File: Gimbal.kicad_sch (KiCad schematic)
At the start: 41 parts, among them J1 Conn_01x03, J2 USB_C_Receptacle_USB2.0, J3 0022232041, J4 0022232041, J5 0022232041, J6 Conn_01x02, Q1 Q_NPN_BCE, Q2 Q_NPN_BCE, SW1 SW_Push, U1 ESP32-WROOM-32U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

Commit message: draft submission
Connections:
- net RX renamed ESPRX
- net ESPRX: now also U3.26 (TXD); no longer U3.25 (RXD)
- net TX renamed ESPTX
- net ESPTX: now also U3.25 (RXD); no longer U3.26 (TXD)
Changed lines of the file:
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@@
     (effects (font (size 1.27 1.27)) (justify left bottom))
   )
-  (label "RX" (at 379.73 134.62 90)
+  (label "ESPRX" (at 379.73 134.62 90)
     (effects (font (size 1.27 1.27)) (justify left bottom))
   )
@@
     (effects (font (size 1.27 1.27)) (justify right bottom))
   )
-  (label "RX" (at 128.27 312.42 0)
+  (label "ESPTX" (at 128.27 312.42 0)
     (effects (font (size 1.27 1.27)) (justify left bottom))
   )
@@
     (effects (font (size 1.27 1.27)) (justify left bottom))
   )
-  (label "TX" (at 71.12 214.63 0)
+  (label "ESPTX" (at 71.12 214.63 0)
     (effects (font (size 1.27 1.27)) (justify left bottom))
   )
@@
     (effects (font (size 1.27 1.27)) (justify left bottom))
   )
-  (label "TX" (at 128.27 309.88 0)
+  (label "ESPRX" (at 128.27 309.88 0)
     (effects (font (size 1.27 1.27)) (justify left bottom))
   )
@@
     (effects (font (size 1.27 1.27)) (justify left bottom))
   )
-  (label "TX" (at 382.27 134.62 90)
+  (label "ESPTX" (at 382.27 134.62 90)
     (effects (font (size 1.27 1.27)) (justify left bottom))
   )
@@
     (effects (font (size 1.27 1.27)) (justify left bottom))
   )
-  (label "RX" (at 71.12 219.71 0)
+  (label "ESPRX" (at 71.12 219.71 0)
     (effects (font (size 1.27 1.27)) (justify left bottom))
   )

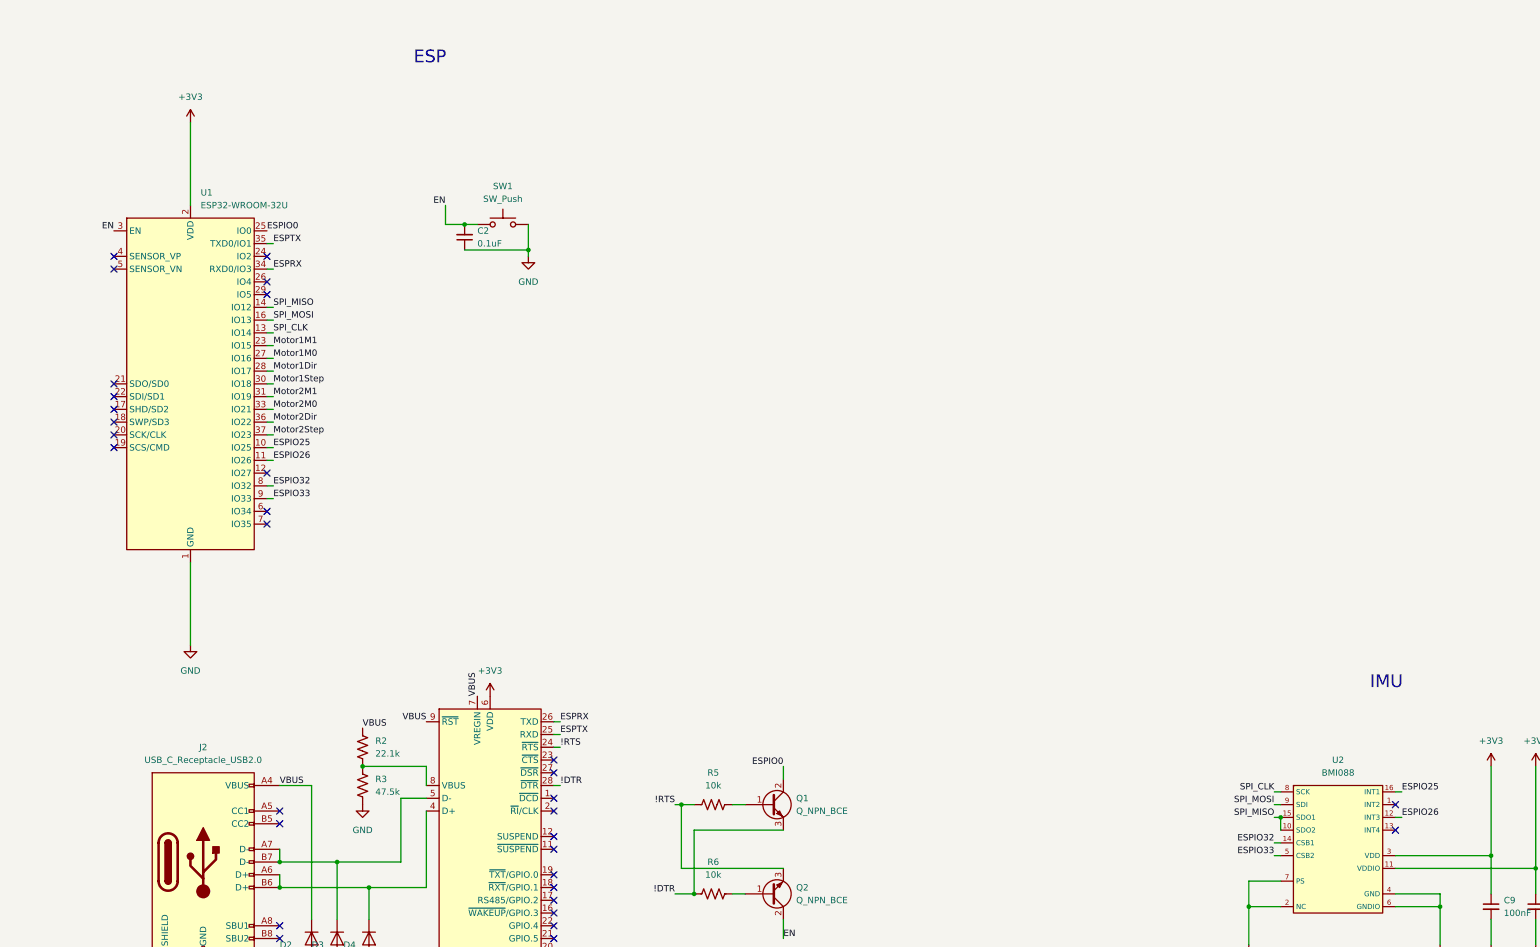
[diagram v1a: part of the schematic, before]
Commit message: changed esp to solo s2
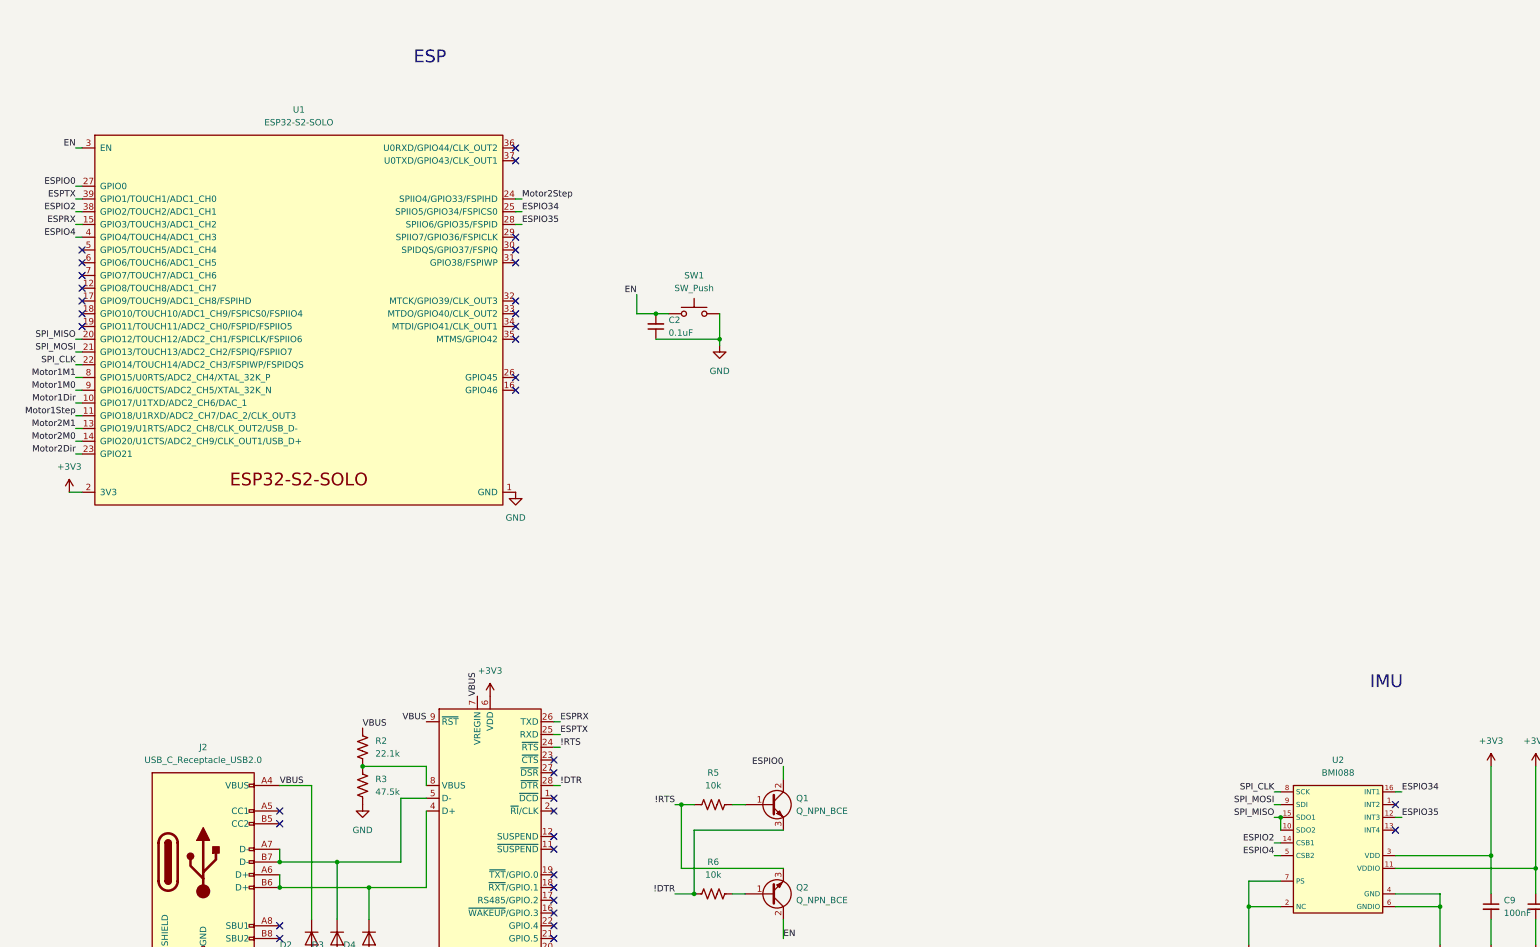
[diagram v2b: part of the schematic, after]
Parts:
- removed U1: ESP32-WROOM-32U, RF_Module:ESP32-WROOM-32U, symbol RF_Module:ESP32-WROOM-32U
- added U1: ESP32-S2-SOLO, Espressif:ESP32-S2-SOLO, symbol Espressif:ESP32-S2-SOLO
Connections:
- net +3V3: now also U1.2 (3V3)
- net EN: now also U1.3 (EN)
- net ESPIO0: now also U1.27 (GPIO0)
- net ESPRX: now also U1.15 (GPIO3/TOUCH3/ADC1_CH2)
- net ESPTX: now also U1.39 (GPIO1/TOUCH1/ADC1_CH0)
- net GND: now also U1.1 (GND), U1.40 (GND), U1.41 (GND)
- net Motor1Dir: now also U1.10 (GPIO17/U1TXD/ADC2_CH6/DAC_1)
- net Motor1M0: now also U1.9 (GPIO16/U0CTS/ADC2_CH5/XTAL_32K_N)
- net Motor1M1: now also U1.8 (GPIO15/U0RTS/ADC2_CH4/XTAL_32K_P)
- net Motor1Step: now also U1.11 (GPIO18/U1RXD/ADC2_CH7/DAC_2/CLK_OUT3)
- net Motor2Dir: now also U1.23 (GPIO21)
- net Motor2M0: now also U1.14 (GPIO20/U1CTS/ADC2_CH9/CLK_OUT1/USB_D+)
- net Motor2M1: now also U1.13 (GPIO19/U1RTS/ADC2_CH8/CLK_OUT2/USB_D-)
- net Motor2Step: now also U1.24 (SPIIO4/GPIO33/FSPIHD)
- net SPI_CLK: now also U1.22 (GPIO14/TOUCH14/ADC2_CH3/FSPIWP/FSPIDQS)
- net SPI_MISO: now also U1.20 (GPIO12/TOUCH12/ADC2_CH1/FSPICLK/FSPIIO6)
- net SPI_MOSI: now also U1.21 (GPIO13/TOUCH13/ADC2_CH2/FSPIQ/FSPIIO7)
- net ESPIO25 renamed ESPIO34
- net ESPIO34: now also U1.25 (SPIIO5/GPIO34/FSPICS0)
- net ESPIO26 renamed ESPIO35
- net ESPIO35: now also U1.28 (SPIIO6/GPIO35/FSPID)
- net ESPIO32 renamed ESPIO2
- net ESPIO2: now also U1.38 (GPIO2/TOUCH2/ADC1_CH1)
- net ESPIO33 renamed ESPIO4
- net ESPIO4: now also U1.4 (GPIO4/TOUCH4/ADC1_CH3)
- no-connect marks 54 -> 58
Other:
- moved on the sheet: C2, SW1

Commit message: assigned all footprints
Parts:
- C1, C10, C11, C2, C3, C4, C5, C6, C7, C8, C9: footprint (none) -> Capacitor_SMD:C_0805_2012Metric
- D1: footprint (none) -> Diode_SMD:D_SOD-323
- D2, D3, D4: footprint (none) -> Package_TO_SOT_SMD:SOT-143
- D5: footprint (none) -> LED_SMD:LED_0805_2012Metric
- J1: footprint (none) -> Connector_Molex:Molex_Micro-Fit_3.0_43650-0300_1x03_P3.00mm_Horizontal
- J2: footprint (none) -> Connector_USB:USB_C_Receptacle_Amphenol_12401548E4-2A
- J3, J4: footprint digikey-footprints:PinHeader_1x4_P2.54mm_Drill1.02mm -> Connector_Molex:Molex_KK-396_A-41791-0004_1x04_P3.96mm_Vertical
- J5: footprint digikey-footprints:PinHeader_1x4_P2.54mm_Drill1.02mm -> Connector_PinHeader_1.00mm:PinHeader_1x04_P1.00mm_Horizontal
- J6: footprint (none) -> Connector_PinHeader_1.00mm:PinHeader_1x02_P1.00mm_Horizontal
- Q1, Q2, U4: footprint (none) -> Package_TO_SOT_SMD:TSOT-23
- R1, R10, R2, R3, R4, R5, R6, R7, R8, R9: footprint (none) -> Resistor_SMD:R_0805_2012Metric
- SW1: footprint (none) -> Button_Switch_SMD:SW_Push_1P1T_NO_CK_KMR2
- U1: footprint Espressif:ESP32-S2-SOLO -> ESP32:ESP32-S2-SOLO
- U5, U6: footprint (none) -> DRV8846RGET:QFN50P400X400X100-25N

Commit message: routing actually good
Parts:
- J2: footprint Connector_USB:USB_C_Receptacle_Amphenol_12401548E4-2A -> Connector_USB:USB_C_Receptacle_Amphenol_12401610E4-2A
- J5: footprint Connector_PinHeader_1.00mm:PinHeader_1x04_P1.00mm_Horizontal -> Connector_PinHeader_2.00mm:PinHeader_1x04_P2.00mm_Horizontal
- J6: footprint Connector_PinHeader_1.00mm:PinHeader_1x02_P1.00mm_Horizontal -> Connector_PinHeader_2.00mm:PinHeader_1x02_P2.00mm_Horizontal
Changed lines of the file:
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@@
     (property "Reference" "J5" (id 0) (at 361.95 143.51 0))
     (property "Value" "0022232041" (id 1) (at 361.95 146.05 0))
-    (property "Footprint" "Connector_PinHeader_1.00mm:PinHeader_1x04_P1.00mm_Horizontal" (id 2) (at 363.22 133.35 0)
+    (property "Footprint" "Connector_PinHeader_2.00mm:PinHeader_1x04_P2.00mm_Horizontal" (id 2) (at 363.22 133.35 0)
       (effects (font (size 1.524 1.524)) (justify left) hide)
     )
@@
       (effects (font (size 1.27 1.27)) (justify left))
     )
-    (property "Footprint" "Connector_PinHeader_1.00mm:PinHeader_1x02_P1.00mm_Horizontal" (id 2) (at 382.27 139.7 0)
+    (property "Footprint" "Connector_PinHeader_2.00mm:PinHeader_1x02_P2.00mm_Horizontal" (id 2) (at 382.27 139.7 0)
       (effects (font (size 1.27 1.27)) hide)
     )
@@
     (property "Reference" "J2" (id 0) (at 57.15 314.96 0))
     (property "Value" "USB_C_Receptacle_USB2.0" (id 1) (at 57.15 317.5 0))
-    (property "Footprint" "Connector_USB:USB_C_Receptacle_Amphenol_12401548E4-2A" (id 2) (at 60.96 337.82 0)
+    (property "Footprint" "Connector_USB:USB_C_Receptacle_Amphenol_12401610E4-2A" (id 2) (at 60.96 337.82 0)
       (effects (font (size 1.27 1.27)) hide)
     )
@@
     )
     (path "/fea1b2d6-14bd-42c1-b173-7589da50729c"
-      (reference "J2") (unit 1) (value "USB_C_Receptacle_USB2.0") (footprint "Connector_USB:USB_C_Receptacle_Amphenol_12401548E4-2A")
+      (reference "J2") (unit 1) (value "USB_C_Receptacle_USB2.0") (footprint "Connector_USB:USB_C_Receptacle_Amphenol_12401610E4-2A")
     )
     (path "/74ab90dc-5bb1-43a8-b284-592b8a08facf"
@@
     )
     (path "/3aa960a7-fd3e-4e4f-9969-73f798fee9d8"
-      (reference "J5") (unit 1) (value "0022232041") (footprint "Connector_PinHeader_1.00mm:PinHeader_1x04_P1.00mm_Horizontal")
+      (reference "J5") (unit 1) (value "0022232041") (footprint "Connector_PinHeader_2.00mm:PinHeader_1x04_P2.00mm_Horizontal")
     )
     (path "/edaf7130-650f-465e-ad0d-68c5743db343"
-      (reference "J6") (unit 1) (value "Conn_01x02") (footprint "Connector_PinHeader_1.00mm:PinHeader_1x02_P1.00mm_Horizontal")
+      (reference "J6") (unit 1) (value "Conn_01x02") (footprint "Connector_PinHeader_2.00mm:PinHeader_1x02_P2.00mm_Horizontal")
     )
     (path "/0263937c-fc21-468b-8423-5c4cfc58d4c0"

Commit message: new schematic
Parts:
- removed D3, D4: DIODE, Package_TO_SOT_SMD:SOT-143, symbol Simulation_SPICE:DIODE
- removed J1: Conn_01x03, Connector_Molex:Molex_Micro-Fit_3.0_43650-0300_1x03_P3.00mm_Horizontal, symbol Connector_Generic:Conn_01x03
- removed Q1, Q2: Q_NPN_BCE, Package_TO_SOT_SMD:TSOT-23, symbol Device:Q_NPN_BCE
- removed R5, R6: 10k, Resistor_SMD:R_0805_2012Metric, symbol Device:R_US
- removed U3: CP2102N-Axx-xQFN28, Package_DFN_QFN:QFN-28-1EP_5x5mm_P0.5mm_EP3.35x3.35mm, symbol Interface_USB:CP2102N-Axx-xQFN28
- added C12, C13, C14: 15uF, Capacitor_SMD:C_0805_2012Metric, symbol Device:C_Small
- added C15: 0.47 uF, Capacitor_SMD:C_0805_2012Metric, symbol Device:C_Small
- added C16: .01uF, Capacitor_SMD:C_0805_2012Metric, symbol Device:C_Small
- added C17, C18: 180uF, Capacitor_SMD:C_0805_2012Metric, symbol Device:C_Small
- added J1: XT60-M, AMASS_XT60-M, symbol GIMBAL:XT60-M
- added L1: 22uH, symbol pspice:INDUCTOR
- added U3: LM2679SX-12, symbol GIMBAL:LM2679SX-12
- D2: footprint Package_TO_SOT_SMD:SOT-143 -> (none)
- R2: value 22.1k -> 5.6k
- R3: value 47.5k -> 10k; footprint Resistor_SMD:R_0805_2012Metric -> (none)
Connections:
- net +12V: now also C17.1, C18.1, L1.2, U3.3 (CB); no longer D1.1 (K)
- net +3V3: now also R3.1
- net EN: now also R3.2
- net GND: now also R2.1, C12.2, C13.2, C14.2, C15.2, C17.2, C18.2, J1.N (NEG), U3.4 (GND); no longer R3.2
- net Motor1Dir: now also U1.7 (GPIO7/TOUCH7/ADC1_CH6); no longer U1.10 (GPIO17/U1TXD/ADC2_CH6/DAC_1)
- net Motor1M0: now also U1.6 (GPIO6/TOUCH6/ADC1_CH5); no longer U1.9 (GPIO16/U0CTS/ADC2_CH5/XTAL_32K_N)
- net Motor1M1: now also U1.5 (GPIO5/TOUCH5/ADC1_CH4); no longer U1.8 (GPIO15/U0RTS/ADC2_CH4/XTAL_32K_P)
- net Motor1Step: now also U1.12 (GPIO8/TOUCH8/ADC1_CH7); no longer U1.11 (GPIO18/U1RXD/ADC2_CH7/DAC_2/CLK_OUT3)
- net Motor2Dir: now also U1.19 (GPIO11/TOUCH11/ADC2_CH0/FSPID/FSPIIO5); no longer U1.23 (GPIO21)
- net Motor2M0: now also U1.18 (GPIO10/TOUCH10/ADC1_CH9/FSPICS0/FSPIIO4); no longer U1.14 (GPIO20/U1CTS/ADC2_CH9/CLK_OUT1/USB_D+)
- net Motor2M1: now also U1.17 (GPIO9/TOUCH9/ADC1_CH8/FSPIHD); no longer U1.13 (GPIO19/U1RTS/ADC2_CH8/CLK_OUT2/USB_D-)
- net Motor2Step: now also U1.8 (GPIO15/U0RTS/ADC2_CH4/XTAL_32K_P); no longer U1.24 (SPIIO4/GPIO33/FSPIHD)
- net at R2.2: now also U3.5 (CURRENT_ADJ); no longer R3.1
- net D+: now reaches J2.A6 (D+), J2.B6 (D+)
- net D+: now also U1.14 (GPIO20/U1CTS/ADC2_CH9/CLK_OUT1/USB_D+)
- net D-: now reaches J2.A7 (D-), J2.B7 (D-)
- net D-: now also U1.13 (GPIO19/U1RTS/ADC2_CH8/CLK_OUT2/USB_D-)
- net +BATT: now reaches D1.2 (A)
- net +BATT: now also D1.1 (K), C12.1, C13.1, C14.1, C15.1, J1.P (POS), U3.2 (INPUT)
- net VBUS: no longer names the net of J2.A4 (VBUS), J2.A9 (VBUS), J2.B4 (VBUS), J2.B9 (VBUS)
- net VBUS: no longer D2.2 (K), R2.1
- new net: C16.2, D2.2 (K), L1.1, U3.1 (SWITCH_OUTPUT)
- new net BUCKCB: C16.1
- new net BUCKFB: U3.6 (FB)
- no-connect marks 58 -> 41
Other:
- moved on the sheet: C1, C3, D1, D5, R4, U4

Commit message: started new layout
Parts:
- added C19: 0.1uF, Capacitor_SMD:C_0805_2012Metric, symbol Device:C_Small
- added R5: 10k, Resistor_SMD:R_0805_2012Metric, symbol Device:R_US
- added SW2: SW_Push, Button_Switch_SMD:SW_Push_1P1T_NO_CK_KMR2, symbol Switch:SW_Push
- C17, C18: footprint Capacitor_SMD:C_0805_2012Metric -> Capacitor_THT:CP_Radial_D8.0mm_P5.00mm
- D2: footprint (none) -> Diode_SMD:D_SMC
- J1: footprint AMASS_XT60-M -> GIMBAL:AMASS_XT60-M
- J5: footprint Connector_PinHeader_2.00mm:PinHeader_1x04_P2.00mm_Horizontal -> Connector_PinHeader_2.00mm:PinHeader_1x04_P2.00mm_Vertical
- J6: footprint Connector_PinHeader_2.00mm:PinHeader_1x02_P2.00mm_Horizontal -> Connector_PinHeader_2.00mm:PinHeader_1x02_P2.00mm_Vertical
- L1: footprint (none) -> Inductor_SMD:L_10.4x10.4_H4.8
- R3: footprint (none) -> Resistor_SMD:R_0805_2012Metric
- U3: footprint (none) -> Package_TO_SOT_SMD:TO-263-7_TabPin8
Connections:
- net BUCKFB is gone; now on net +12V: U3.6 (FB)
- net +12V: no longer U3.3 (CB)
- net +3V3: now also R5.1
- net +BATT: no longer D1.2 (A), J1.P (POS)
- net BUCKCB: now also U3.3 (CB)
- net GND: now also C19.1, SW2.2
- new net: D1.2 (A), J1.P (POS)
- new net GPIO0: C19.2, R5.2, SW2.1
